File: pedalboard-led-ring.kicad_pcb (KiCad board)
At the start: 2 copper layers, 24 x 24 mm, 33 parts, among them J1 middle, J2 edge

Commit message: Simplificaitons
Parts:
- removed H1, H2, H3: MountingHole, MountingHole:MountingHole_2.2mm_M2
- removed J2: edge, Connector_PinSocket_2.00mm:PinSocket_2x02_P2.00mm_Vertical_SMD
- removed R2: 0, Resistor_SMD:R_0201_0603Metric_Pad0.64x0.40mm_HandSolder
- added JP1: SJ, Jumper:SolderJumper-2_P1.3mm_Bridged_RoundedPad1.0x1.5mm, B.Cu at (85.8, 54.2)
- moved C10 0.17 mm to (81.5, 69.0)
- moved C5 0.17 mm to (74.2, 52.9)
- moved C7 0.16 mm to (71.0, 61.5)
- moved C11 0.16 mm to (85.8, 67.1)
- moved C4 0.15 mm to (78.5, 51.1)
- moved C12 0.14 mm to (88.5, 63.2)
- moved C6 0.13 mm to (71.5, 56.8)
- moved C9 0.13 mm to (76.8, 68.5)
- moved C3 0.13 mm to (83.2, 51.5)
- moved C2 0.13 mm to (87.0, 54.2)
- moved C8 0.13 mm to (73.0, 65.8)
- moved D13 0.09 mm to (88.8, 57.2), turned to 90 degrees
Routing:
- net Net-(J1-Pin_3): track 16.6 -> 6.09 mm
- net Net-(D12-DOUT): track 8.93 -> 3.08 mm
- net GND: track 11.3 -> 5.97 mm, vias 8 -> 4
- net Net-(D1-VDD): track 2.76 -> 7.63 mm, vias 0 -> 1
- net Net-(D1-DOUT): track 4.66 -> 5.64 mm
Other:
- outline, holes or cut-outs redrawn
- board text removed: "DO"

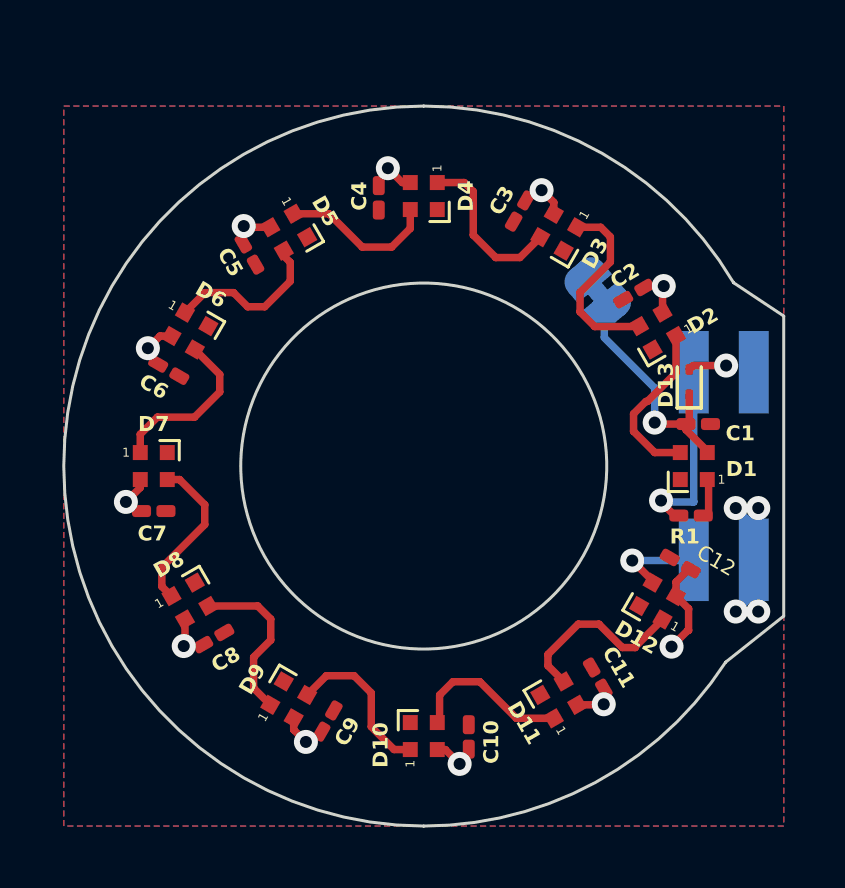
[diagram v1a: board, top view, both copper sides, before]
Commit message: Add fiducials for p&p
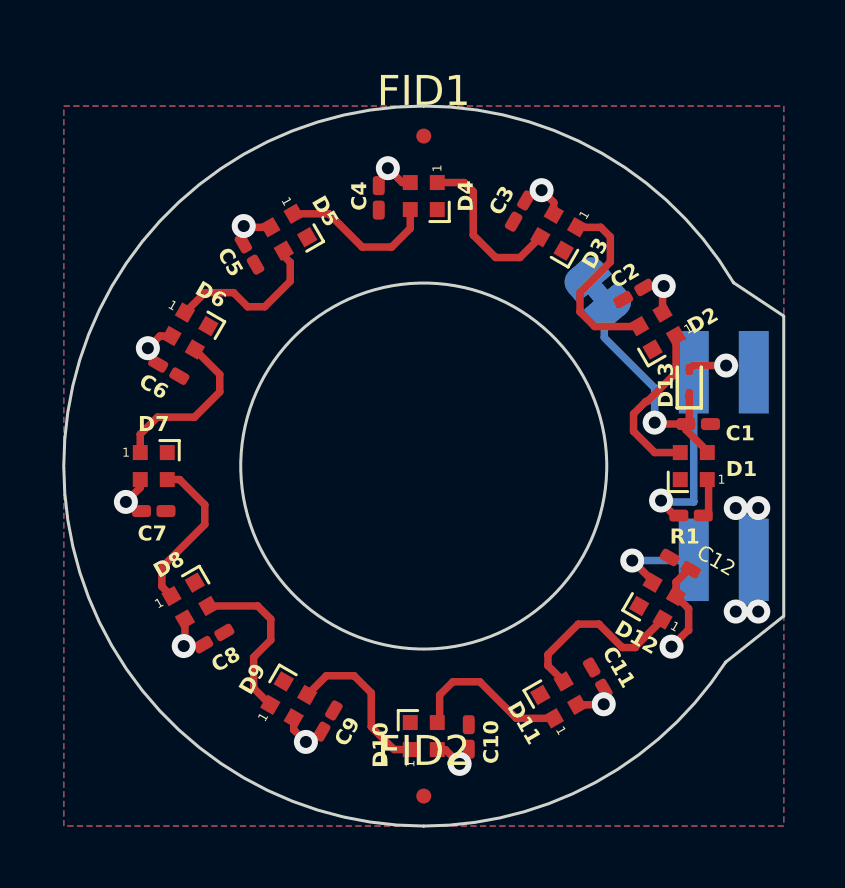
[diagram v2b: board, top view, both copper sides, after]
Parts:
- added FID1: Fiducial, Fiducial:Fiducial_0.5mm_Mask1mm, F.Cu at (80.0, 49.0)
- added FID2: Fiducial, Fiducial:Fiducial_0.5mm_Mask1mm, F.Cu at (80.0, 71.0)
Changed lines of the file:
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@@
   (net 16 "Net-(D1-VDD)")
   (net 17 "Net-(J1-Pin_3)")
+  (footprint "Fiducial:Fiducial_0.5mm_Mask1mm" (layer "F.Cu")
+    (at 80 71)
+    (descr "Circular Fiducial, 0.5mm bare copper, 1mm soldermask opening (Level C)")
+    (tags "fiducial")
+    (property "Sheetfile" "pedalboard-led-ring.kicad_sch")
+    (property "Sheetname" "")
+    (property "ki_description" "Fiducial Marker")
+    (property "ki_keywords" "fiducial marker")
+    (attr smd)
+    (fp_text reference "FID2" (at 0 -1.5) (layer "F.SilkS")
+        (effects (font (size 1 1) (thickness 0.15)))
+    )
+    (fp_text value "Fiducial" (at 0 1.5) (layer "F.Fab")
+        (effects (font (size 1 1) (thickness 0.15)))
+    )
+    (fp_text user "${REFERENCE}" (at 0 0) (layer "F.Fab")
+        (effects (font (size 0.2 0.2) (thickness 0.04)))
+    )
+    (fp_circle (center 0 0) (end 0.75 0)
+      (stroke (width 0.05) (type solid)) (fill none) (layer "F.CrtYd"))
+    (fp_circle (center 0 0) (end 0.5 0)
+      (stroke (width 0.1) (type solid)) (fill none) (layer "F.Fab"))
+    (pad "" smd circle (at 0 0) (size 0.5 0.5) (layers "F.Cu" "F.Mask")
+      (solder_mask_margin 0.25) (clearance 0.25))
+  )
   (footprint "Library:LED_SK6812_EC15_1.5x1.5mm" (layer "F.Cu")
     (at 84.5 67.794229 120)
@@
     )
   )
+  (footprint "Fiducial:Fiducial_0.5mm_Mask1mm" (layer "F.Cu")
+    (at 80 49)
+    (descr "Circular Fiducial, 0.5mm bare copper, 1mm soldermask opening (Level C)")
+    (tags "fiducial")
+    (property "Sheetfile" "pedalboard-led-ring.kicad_sch")
+    (property "Sheetname" "")
+    (property "ki_description" "Fiducial Marker")
+    (property "ki_keywords" "fiducial marker")
+    (attr smd)
+    (fp_text reference "FID1" (at 0 -1.5) (layer "F.SilkS")
+        (effects (font (size 1 1) (thickness 0.15)))
+    )
+    (fp_text value "Fiducial" (at 0 1.5) (layer "F.Fab")
+        (effects (font (size 1 1) (thickness 0.15)))
+    )
+    (fp_text user "${REFERENCE}" (at 0 0) (layer "F.Fab")
+        (effects (font (size 0.2 0.2) (thickness 0.04)))
+    )
+    (fp_circle (center 0 0) (end 0.75 0)
+      (stroke (width 0.05) (type solid)) (fill none) (layer "F.CrtYd"))
+    (fp_circle (center 0 0) (end 0.5 0)
+      (stroke (width 0.1) (type solid)) (fill none) (layer "F.Fab"))
+    (pad "" smd circle (at 0 0) (size 0.5 0.5) (layers "F.Cu" "F.Mask")
+      (solder_mask_margin 0.25) (clearance 0.25))
+  )
   (footprint "Capacitor_SMD:C_0201_0603Metric_Pad0.64x0.40mm_HandSolder" (layer "F.Cu")

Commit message: Change to 0402 components
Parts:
- C1, C10, C11, C12, C2, C3, C4, C5, C6, C7, C8, C9: footprint Capacitor_SMD:C_0201_0603Metric_Pad0.64x0.40mm_HandSolder -> Capacitor_SMD:C_0402_1005Metric
- J1: value middle -> 02x02
- R1: footprint Resistor_SMD:R_0201_0603Metric_Pad0.64x0.40mm_HandSolder -> Resistor_SMD:R_0402_1005Metric
- moved C1 0.07 mm to (89.2, 58.5)
- moved D13 0.05 mm to (88.8, 57.1)

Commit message: Add additional Fiducial
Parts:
- added FID3: Fiducial, Fiducial:Fiducial_0.5mm_Mask1mm, F.Cu at (69.0, 60.0)
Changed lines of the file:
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@@
     (property "ki_keywords" "fiducial marker")
     (attr smd)
-    (fp_text reference "FID2" (at -2.6 -0.16) (layer "F.SilkS")
+    (fp_text reference "FID2" (at -1.96 -0.03) (layer "F.SilkS")
         (effects (font (size 0.5 0.5) (thickness 0.1) bold))
     )
@@
     (property "ki_keywords" "fiducial marker")
     (attr smd)
-    (fp_text reference "FID1" (at -1.67 -0.22) (layer "F.SilkS")
+    (fp_text reference "FID1" (at -1.67 0) (layer "F.SilkS")
         (effects (font (size 0.5 0.5) (thickness 0.1) bold))
     )
@@
     )
   )
+  (footprint "Fiducial:Fiducial_0.5mm_Mask1mm" (layer "F.Cu")
+    (at 69 60)
+    (descr "Circular Fiducial, 0.5mm bare copper, 1mm soldermask opening (Level C)")
+    (tags "fiducial")
+    (property "Sheetfile" "pedalboard-led-ring.kicad_sch")
+    (property "Sheetname" "")
+    (property "ki_description" "Fiducial Marker")
+    (property "ki_keywords" "fiducial marker")
+    (attr smd)
+    (fp_text reference "FID3" (at 0 -1.5) (layer "F.SilkS")
+        (effects (font (size 0.5 0.5) (thickness 0.1) bold))
+    )
+    (fp_text value "Fiducial" (at 0 1.5) (layer "F.Fab")
+        (effects (font (size 1 1) (thickness 0.15)))
+    )
+    (fp_text user "${REFERENCE}" (at 0 0) (layer "F.Fab")
+        (effects (font (size 0.2 0.2) (thickness 0.04)))
+    )
+    (fp_circle (center 0 0) (end 0.75 0)
+      (stroke (width 0.05) (type solid)) (fill none) (layer "F.CrtYd"))
+    (fp_circle (center 0 0) (end 0.5 0)
+      (stroke (width 0.1) (type solid)) (fill none) (layer "F.Fab"))
+    (pad "" smd circle (at 0 0) (size 0.5 0.5) (layers "F.Cu" "F.Mask")
+      (solder_mask_margin 0.25) (clearance 0.25))
+  )
   (footprint "Connector_PinSocket_2.00mm:PinSocket_2x02_P2.00mm_Vertical_SMD" (layer "B.Cu")

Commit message: Add GIT_HASH to schema and PCB
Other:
- board text added: "PCB: v${REVISION} {GIT_HASH}"
- board text removed: "PCB: v${REVISION}"
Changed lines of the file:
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@@
     (comment 1 "Source Code: https://github.com/pedalboard/pedalboard-led-ring")
     (comment 2 "License: CERN Open Hardware Licence Version 2 - Permissive")
+    (comment 3 "Git commit: {GIT_HASH}")
   )
   (layers
@@
     (effects (font (size 0.6 0.6) (thickness 0.1)) (justify left bottom mirror))
   )
-  (gr_text "PCB: v${REVISION}" (at 79.66 71.13) (layer "B.SilkS")
+  (gr_text "PCB: v${REVISION} \n{GIT_HASH}" (at 79.95 70.64) (layer "B.SilkS")
     (effects (font (size 0.5 0.5) (thickness 0.1) bold) (justify bottom mirror))
   )

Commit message: Fix GIT_HASH references
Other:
- board text added: "PCB: v${REVISION} $:${GIT_HASH}"
- board text removed: "PCB: v${REVISION} {GIT_HASH}"
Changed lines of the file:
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@@
     (comment 1 "Source Code: https://github.com/pedalboard/pedalboard-led-ring")
     (comment 2 "License: CERN Open Hardware Licence Version 2 - Permissive")
-    (comment 3 "Git commit: {GIT_HASH}")
+    (comment 3 "Git commit: ${GIT_HASH}")
   )
   (layers
@@
     (effects (font (size 0.6 0.6) (thickness 0.1)) (justify left bottom mirror))
   )
-  (gr_text "PCB: v${REVISION} \n{GIT_HASH}" (at 79.95 70.64) (layer "B.SilkS")
+  (gr_text "PCB: v${REVISION} \n$:${GIT_HASH}" (at 79.95 70.64) (layer "B.SilkS")
     (effects (font (size 0.5 0.5) (thickness 0.1) bold) (justify bottom mirror))
   )
